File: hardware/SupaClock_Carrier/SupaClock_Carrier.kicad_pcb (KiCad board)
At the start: 2 copper layers, 85 x 67 mm, 25 parts, among them J11 AD8232_SparkFun, J12_LA1 ECG_LA_pad_M3, J12_RA1 ECG_RA_pad_M3, J12_RL1 ECG_RL_pad_M3, J13 AD8232_Pads_RA_LA_RL, J14 MAX30102_bot, J15 XIAO_BAT_Wires, J3 MAX30102_top, J4 MAX30205_8pad, J5 BMI160_7p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

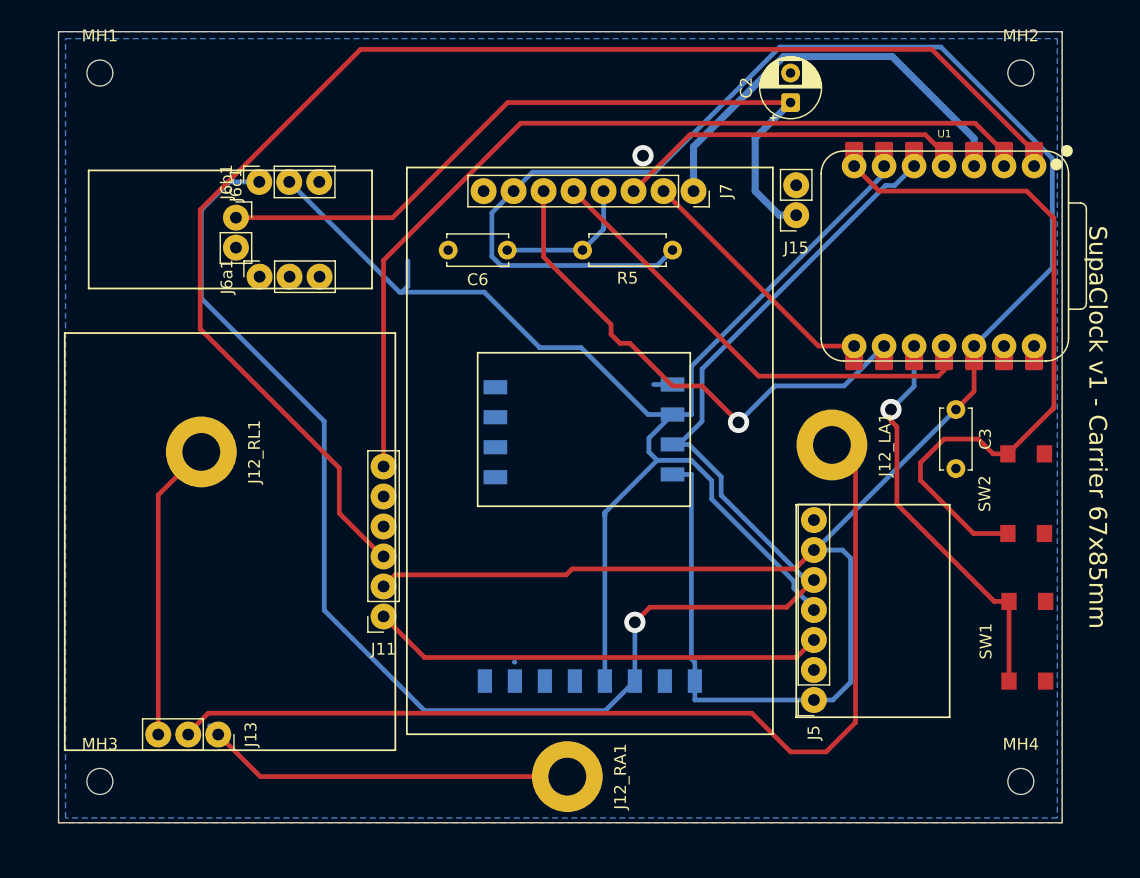
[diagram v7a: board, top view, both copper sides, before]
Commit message: Add new STL file for Supaclock V2 top case
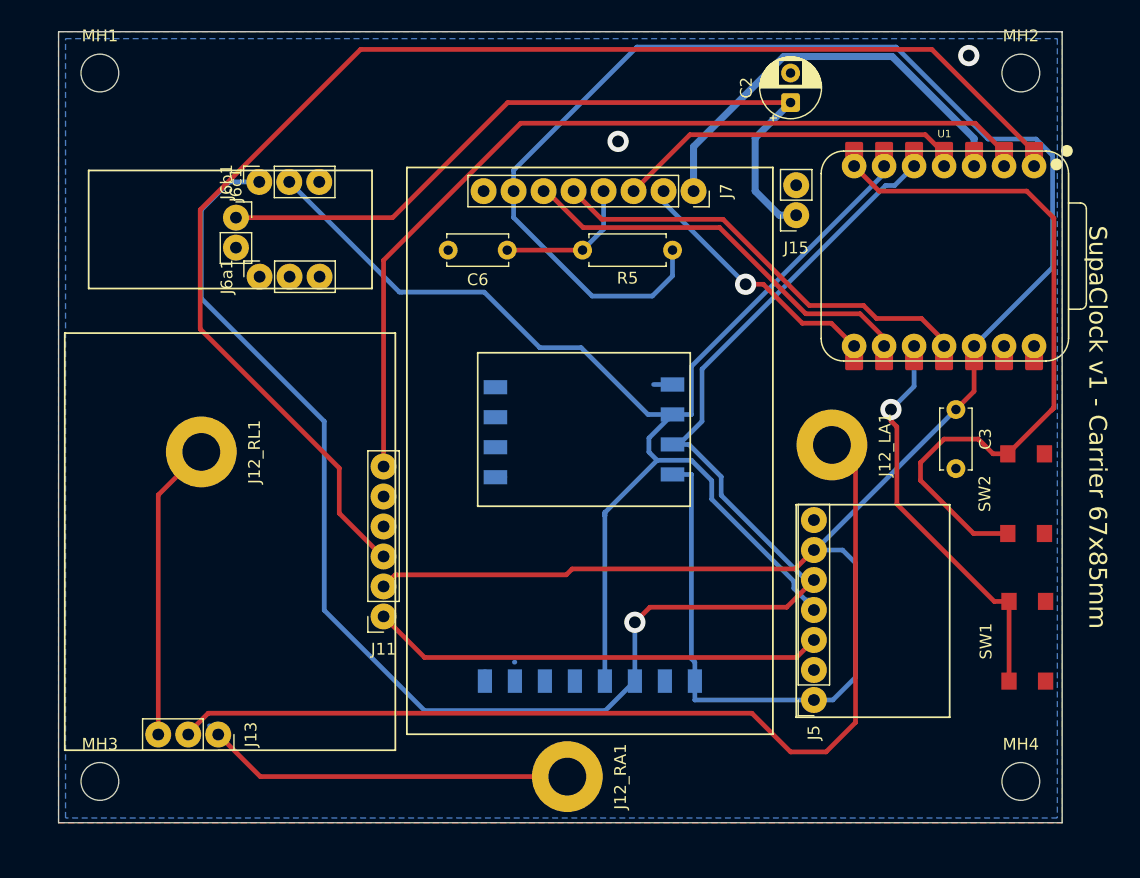
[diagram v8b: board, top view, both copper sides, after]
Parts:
- MH1, MH2, MH3, MH4: value MountingHole_2.2mm_M2 -> MountingHole_3.2mm_M3; footprint MountingHole:MountingHole_2.2mm_M2 -> MountingHole:MountingHole_3.2mm_M3
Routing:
- net /SPI_SCK: track 45.7 -> 34.9 mm, vias 1 -> 0
- net /SPI_MOSI: track 42.2 -> 37.9 mm
- net /I2C_SCL: track 119.9 -> 117.1 mm
- net /+3V3: track 205.5 -> 206.1 mm
- net /SPI_CS: track 22.5 -> 23.0 mm, vias 0 -> 1
- net /GND: vias 1 -> 2
